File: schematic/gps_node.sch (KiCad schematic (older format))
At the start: 54 parts

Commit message: Changed battery measurement
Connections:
- net labels added: V_Batt_input
- wire segments 165 -> 170
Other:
- moved on the sheet: C?, J?, SW?, U?

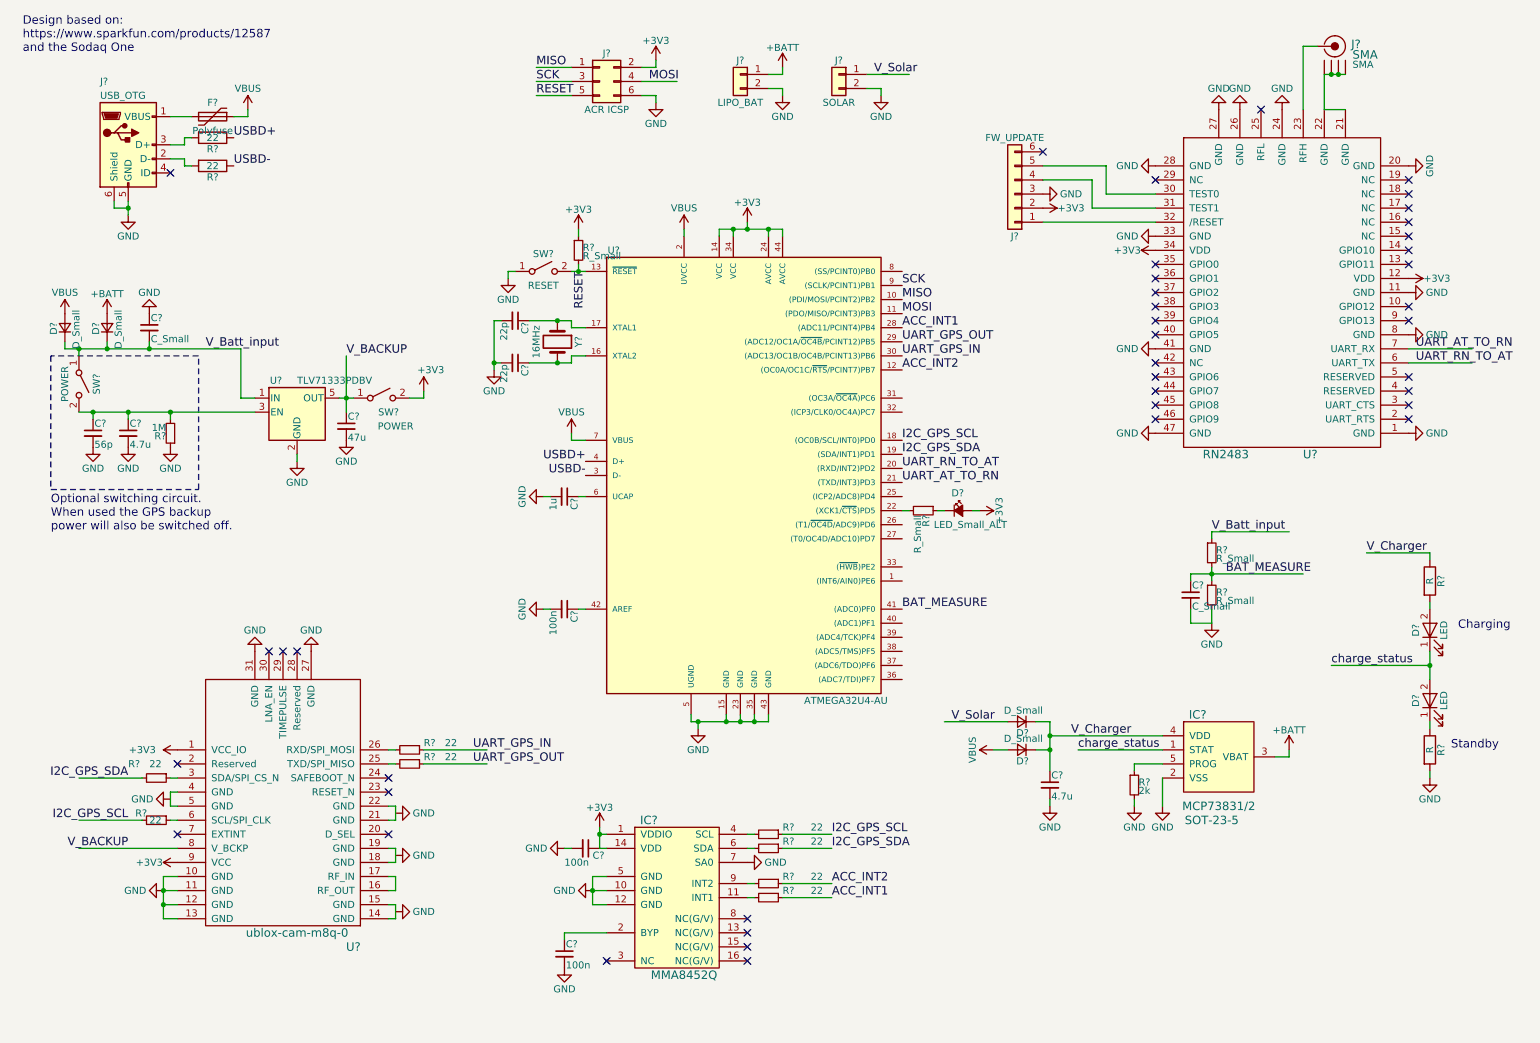
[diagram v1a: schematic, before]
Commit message: Updates to power segment
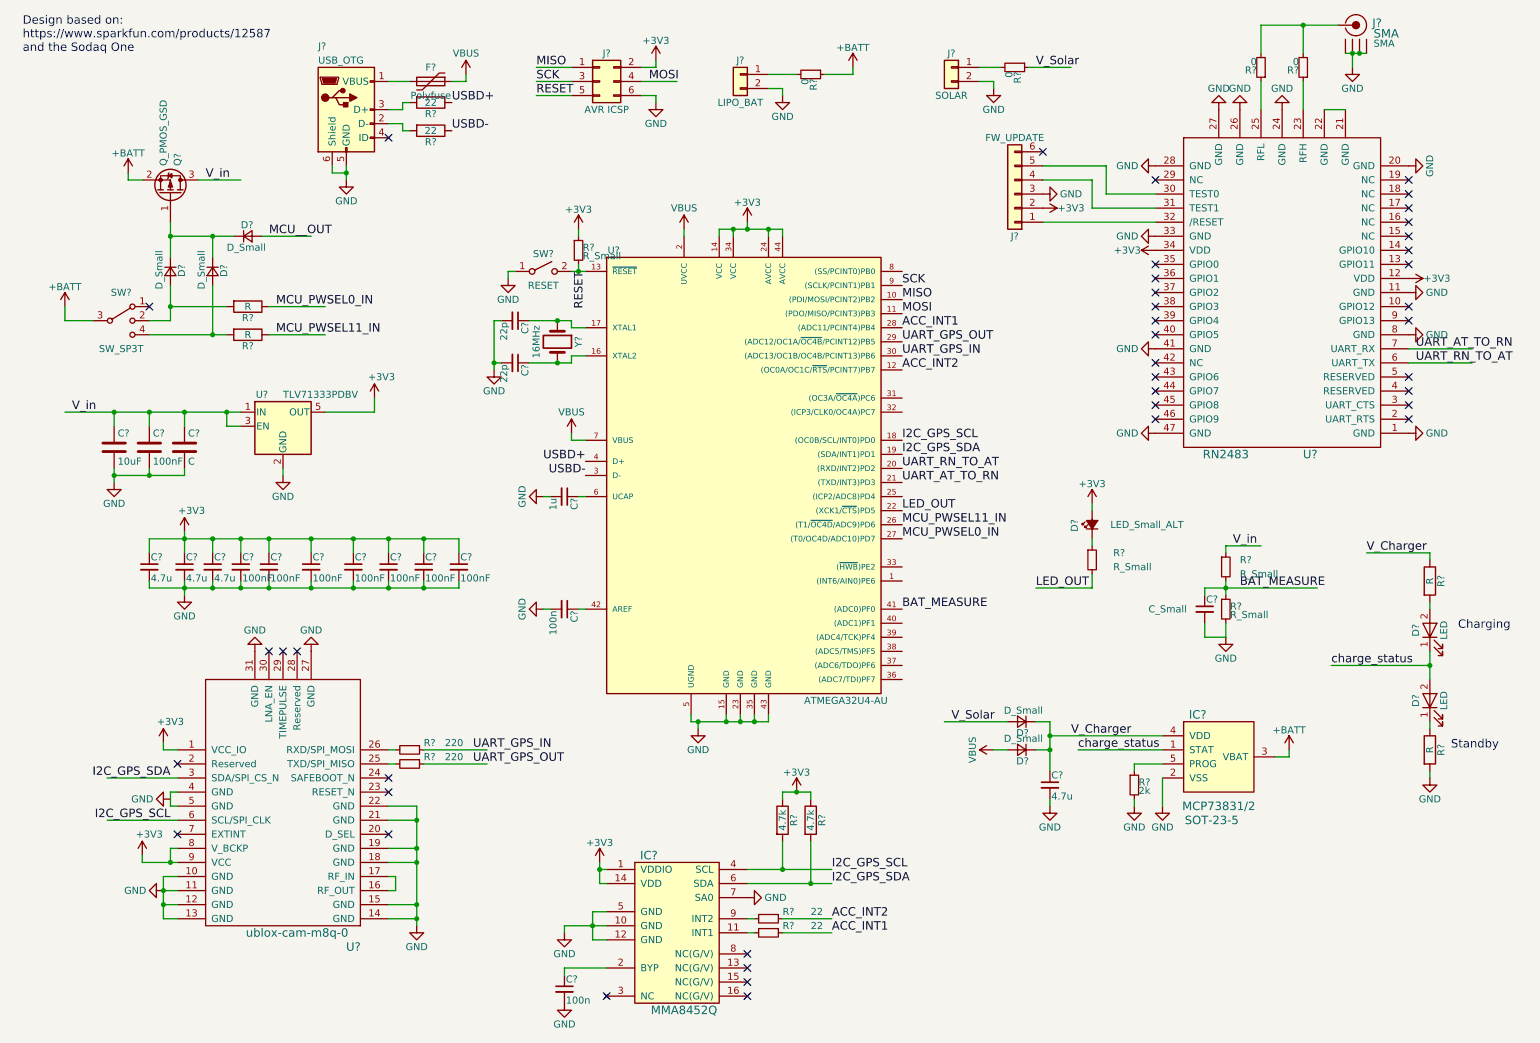
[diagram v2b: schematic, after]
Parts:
- removed C?: C_Small, symbol C_Small
- removed C?: 4.7u, symbol C_Small
- removed C?: 56p, symbol C_Small
- removed C?: 47u, symbol C_Small
- removed C?: 100n, symbol C_Small
- removed D? (x2): D_Small, symbol D_Small
- removed R?: 1M, symbol R_Small
- removed R? (x4): 22, symbol R_Small
- removed SW? (x2): POWER, symbol SW_SPST
- added C?: 10uF, symbol C
- added C?: 100nF, symbol C
- added C?: C, symbol C
- added C? (x3): 4.7u, symbol C_Small
- added C? (x7): 100nF, symbol C_Small
- added D? (x3): D_Small, symbol D_Small
- added Q?: Q_PMOS_GSD, symbol Q_PMOS_GSD
- added R? (x2): R, symbol R
- added R? (x4): 0, symbol R_Small
- added R? (x2): 4.7k, symbol R
- added SW?: SW_SP3T, symbol SW_SP3T
- J?: value ACR ICSP -> AVR ICSP
- R? (x2): value 22 -> 220
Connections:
- net labels added: LED_OUT, MCU_PWSEL0_IN, MCU_PWSEL11_IN, MCU__OUT, V_in
- net labels removed: V_BACKUP, V_Batt_input
- wire segments 170 -> 215
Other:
- note removed: "Optional switching circuit.\nWhen used the GPS backup \npower will also be switched off."
- moved on the sheet: C?, D?, F?, IC?, J?, R?, U?

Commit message: Add test and debug points
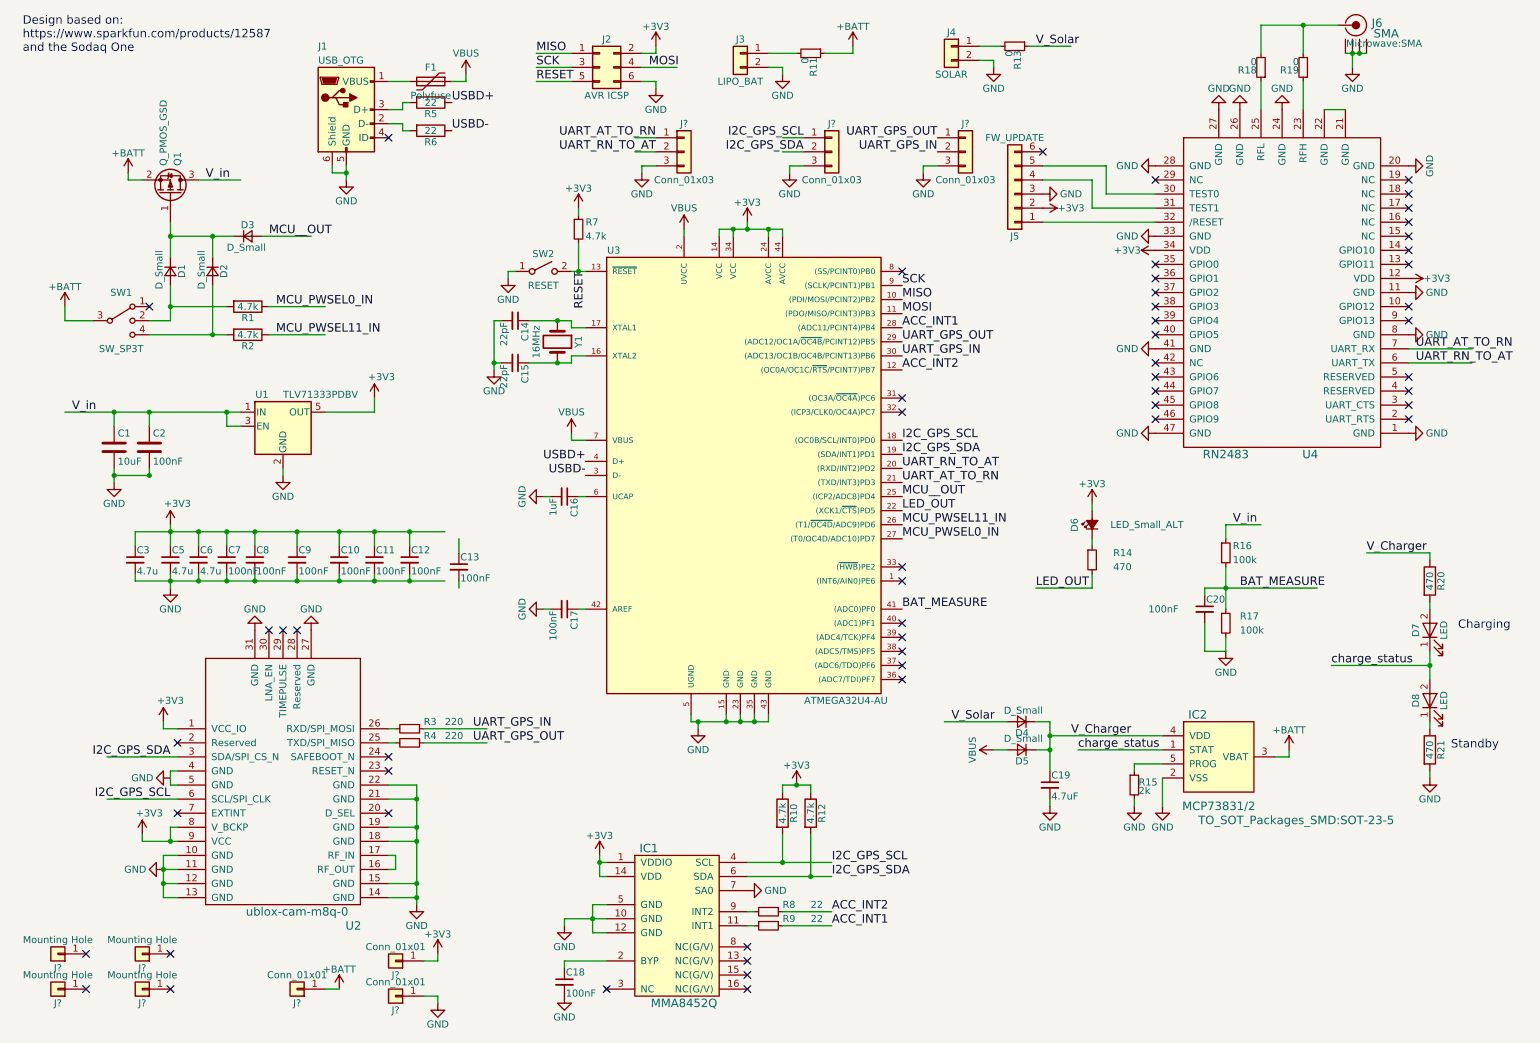
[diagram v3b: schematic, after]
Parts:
- removed C?: C, symbol C
- added J? (x4): Mounting Hole, symbol Conn_01x01
- added J? (x3): Conn_01x01, symbol Conn_01x01
- added J? (x3): Conn_01x03, symbol Conn_01x03
- C1, C10, C11, C12, C13, C2, C3, C5, C6, C7, C8, C9: renamed from C?; footprint (none) -> Capacitors_SMD:C_0805
- C14, C15: renamed from C?; value 22p -> 22pF; footprint (none) -> Capacitors_SMD:C_0805
- C16: renamed from C?; value 1u -> 1uF; footprint (none) -> Capacitors_SMD:C_0805
- C17, C18: renamed from C?; value 100n -> 100nF; footprint (none) -> Capacitors_SMD:C_0805
- C19: renamed from C?; value 4.7u -> 4.7uF; footprint (none) -> Capacitors_SMD:C_0805
- C20: renamed from C?; value C_Small -> 100nF; footprint (none) -> Capacitors_SMD:C_0805
- IC2: renamed from IC?; footprint SOT-23-5 -> TO_SOT_Packages_SMD:SOT-23-5
- J6: renamed from J?; footprint SMA -> Microwave:SMA
- R1, R2: renamed from R?; value R -> 4.7k
- R14: renamed from R?; value R_Small -> 470
- R16, R17: renamed from R?; value R_Small -> 100k
- R20, R21: renamed from R?; value R -> 470
- R7: renamed from R?; value R_Small -> 4.7k
- gave numbers to parts that had none: 36
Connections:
- wire segments 215 -> 228
- no-connect marks 41 -> 55
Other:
- moved on the sheet: C10, C11, C12, C18, C3, C5, C6, C7, C8, C9, IC1, J2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
